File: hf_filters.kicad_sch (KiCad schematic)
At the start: 69 parts, among them J2 FILT_IN, J3 To CTRL:FILT_L, J4 UF1_OUT, J5 UF1_IN, J6 FILT_OUT, K10 EC2-5SNU, K11 EC2-5SNU, K4 EC2-5SNU, K5 EC2-5SNU, K6 EC2-5SNU, K7 EC2-5SNU, K8 EC2-5SNU, K9 EC2-5SNU, U4 ULN2803A, U5 74HC596

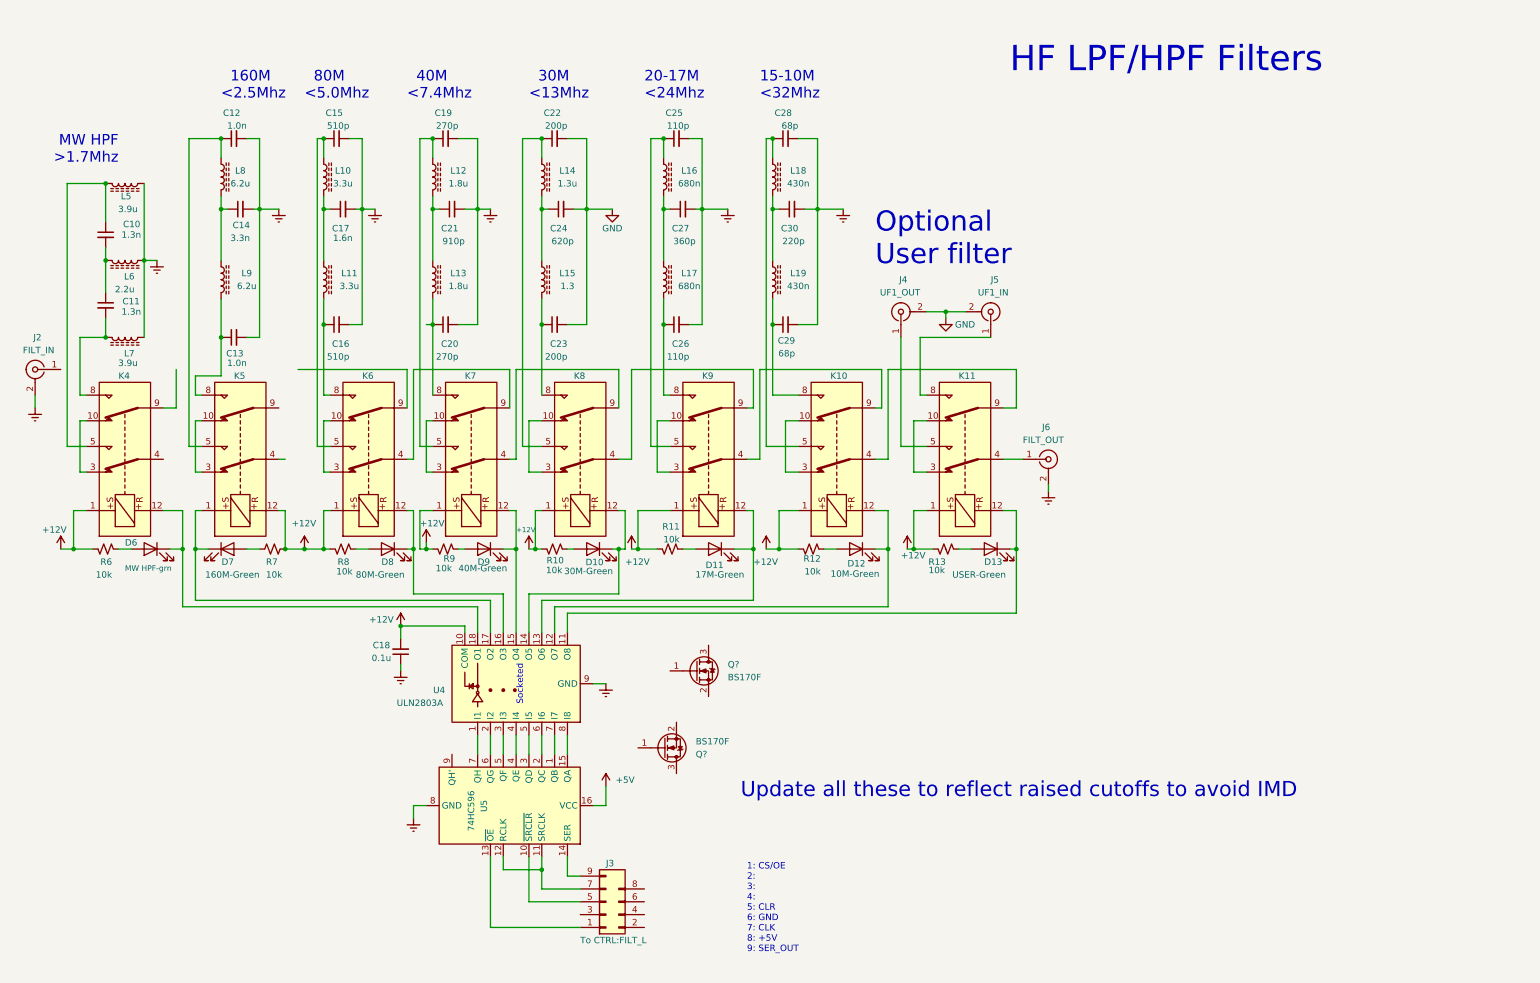
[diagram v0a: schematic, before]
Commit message: Replaced 74hc596 parts with mcp23017 and mcp23008 parts to simplify routing and reduce external parts count.
Added interface connectors for eventualy VHF (6m/2m/1.25m) RF path board.

Attempted to create some sort of documentations...
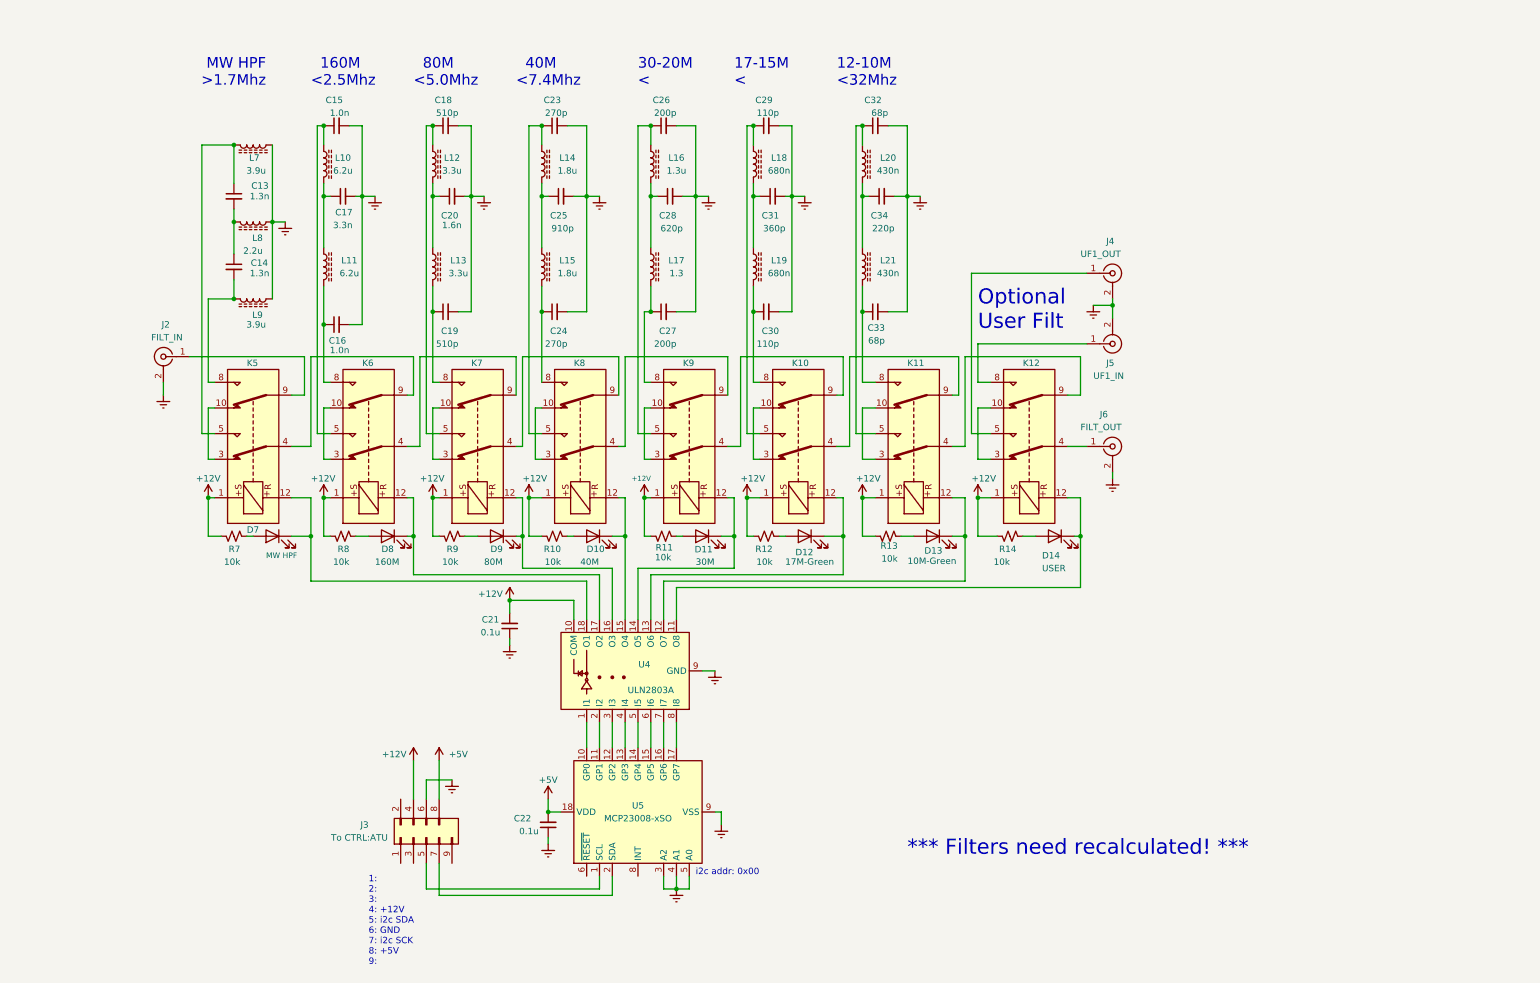
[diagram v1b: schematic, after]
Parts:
- removed Q? (x2): BS170F, Package_TO_SOT_SMD:SOT-23, symbol Transistor_FET:BS170F
- removed U5: 74HC596, Package_SO:TSSOP-16_4.4x5mm_P0.65mm, symbol 74xx:74HC596
- added C22: 0.1u, Capacitor_THT:C_Disc_D4.7mm_W2.5mm_P5.00mm, symbol Device:C_Small
- added U5: MCP23008-xSO, Package_SO:SOIC-18W_7.5x11.6mm_P1.27mm, symbol Interface_Expansion:MCP23008-xSO
- D10: renamed from D9; value 40M-Green -> 40M
- D11: renamed from D10; value 30M-Green -> 30M
- D14: renamed from D13; value USER-Green -> USER
- D7: renamed from D6; value MW HPF-grn -> MW HPF
- D8: renamed from D7; value 160M-Green -> 160M
- D9: renamed from D8; value 80M-Green -> 80M
- J3: value To CTRL:FILT_L -> To CTRL:ATU
- renumbered C10 to C13, C11 to C14, C12 to C15, C13 to C16, C14 to C17, C15 to C18, C16 to C19, C17 to C20, C18 to C21, C19 to C23, C20 to C24, C21 to C25, C22 to C26, C23 to C27, C24 to C28, C25 to C29, C26 to C30, C27 to C31, C28 to C32, C29 to C33, C30 to C34, D11 to D12, D12 to D13, K9 to K10, K10 to K11, K11 to K12, K4 to K5, K5 to K6, K6 to K7, K7 to K8, K8 to K9, L8 to L10, L9 to L11, L10 to L12, L11 to L13, L12 to L14, L13 to L15, L14 to L16, L15 to L17, L16 to L18, L17 to L19, L18 to L20, L19 to L21, L5 to L7, L6 to L8, L7 to L9, R9 to R10, R10 to R11, R11 to R12, R12 to R13, R13 to R14, R6 to R7, R7 to R8, R8 to R9
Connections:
- net GND is gone; now on net Earth: C26.2, C27.2, C28.2, J4.2 (Ext), J5.2 (Ext)
- net +12V: now also J3.4 (Pin_4), K6.1; no longer K6.12
- net +5V: now also J3.8 (Pin_8), C22.2, U5.18 (VDD)
- net Earth: now also J3.6 (Pin_6), C22.1, U5.3 (A2), U5.4 (A1), U5.5 (A0), U5.9 (VSS)
- net at D8.1 (K), U4.17 (O2): now also K6.12; no longer K6.1
- net at K6.4: now also K7.9
- net at K6.9: now also K5.4
- net at U4.7 (I7): now also U5.16 (GP6)
- net at J3.5 (Pin_5): now also U5.1 (SCL)
- net at J3.7 (Pin_7): now also U5.2 (SDA)
- net at U4.8 (I8): now also U5.17 (GP7)
- net at U4.6 (I6): now also U5.15 (GP5)
- net at U4.5 (I5): now also U5.14 (GP4)
- net at U4.4 (I4): now also U5.13 (GP3)
- net at U4.3 (I3): now also U5.12 (GP2)
- net at U4.2 (I2): now also U5.11 (GP1)
- net at U4.1 (I1): now also U5.10 (GP0)
- net at J2.1 (In): now also K5.9
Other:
- note added: "*** Filters need recalculated! ***"
- note added: "12-10M <32Mhz"
- note added: "17-15M <"
- note added: "1: 2: 3: 4: +12V 5: i2c SDA 6: GND 7: i2c SCK 8: +5V 9:"
- note added: "30-20M <"
- note added: "Optional User Filt"
- note added: "i2c addr: 0x00"
- note removed: "15-10M <32Mhz"
- note removed: "1: CS/OE 2: 3: 4: 5: CLR 6: GND 7: CLK 8: +5V 9: SER_OUT"
- note removed: "20-17M <24Mhz"
- note removed: "30M <13Mhz"
- note removed: "HF LPF/HPF Filters"
- note removed: "Optional User filter"
- note removed: "Socketed"
- note removed: "Update all these to reflect raised cutoffs to avoid IMD"
- moved on the sheet: C13, C14, C15, C16, C17, C18, C19, C20, C21, C23, C24, C25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

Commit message: cleanup of schematic and some initial firmware works...
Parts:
- removed C13: 1.3n, symbol Device:C_Small
- removed C22: 0.1u, Capacitor_THT:C_Disc_D4.7mm_W2.5mm_P5.00mm, symbol Device:C_Small
- removed D7: MW HPF, symbol Device:LED
- removed J2: FILT_IN, symbol Connector:Conn_Coaxial
- removed K5: EC2-5SNU, Relay_THT:Relay_DPDT_Kemet_EC2, symbol Relay:EC2-5SNU
- removed L7, L9: 3.9u, symbol Device:L_Ferrite
- removed R7: 10k, symbol Device:R_Small_US
- removed U5: MCP23008-xSO, Package_SO:SOIC-18W_7.5x11.6mm_P1.27mm, symbol Interface_Expansion:MCP23008-xSO
- added C23, C24, C25, C26, C27, C28, C29: 0.1u, Capacitor_THT:C_Disc_D4.7mm_W2.5mm_P5.00mm, symbol Device:C_Small
- added C30, C31, C32, C33, C34, C35, C36, C37, C38, C39, C7: 1.3n, symbol Device:C_Small
- added D1, D62: USER2, symbol Device:LED
- added D10, D11, D12, D13, D9: MW HPF, symbol Device:LED
- added J3: TX_FILT_IN, symbol Connector:Conn_Coaxial
- added J37: UTF2_OUT, symbol Connector:Conn_Coaxial
- added J38: TX_FILT_OUT, symbol Connector:Conn_Coaxial
- added J4: UTF2_IN, symbol Connector:Conn_Coaxial
- added J7: RX_FILT_IN, symbol Connector:Conn_Coaxial
- added K1, K10, K11, K12, K13, K45, K9: EC2-5SNU, Relay_THT:Relay_DPDT_Kemet_EC2, symbol Relay:EC2-5SNU
- added L1, L15, L16, L17, L18, L19, L20, L26, L27, L28, L29, L30: 3.9u, symbol Device:L_Ferrite
- added L21, L22, L23, L24, L25: 2.2u, symbol Device:L_Ferrite
- added R1, R10, R11, R12, R13, R87, R9: 10k, symbol Device:R_Small_US
- added U2: MCP23017_SO, Package_SO:SOIC-28W_7.5x17.9mm_P1.27mm, symbol Interface_Expansion:MCP23017_SO
- added U3: ULN2803A, symbol Transistor_Array:ULN2803A
- D2: renamed from D14; value USER -> USER1
- D3: renamed from D13; value 10M-Green -> 12-10M
- D4: renamed from D12; value 17M-Green -> 17-15M
- D5: renamed from D11; value 30M -> 30-20M
- J1: renamed from J5; value UF1_IN -> UTF1_IN
- J2: renamed from J4; value UF1_OUT -> UTF1_OUT
- J5: renamed from J3; value To CTRL:ATU -> To CTRL_FILT
- J6: value FILT_OUT -> RX_FILT_OUT
- renumbered C32 to C1, C28 to C10, C25 to C11, C20 to C12, C17 to C13, C33 to C15, C30 to C16, C27 to C17, C24 to C18, C29 to C2, C16 to C20, C26 to C3, C23 to C4, C18 to C5, C15 to C6, C34 to C8, C31 to C9, D10 to D6, D9 to D7, K12 to K2, K11 to K3, K10 to K4, K9 to K5, K8 to K6, K6 to K8, L19 to L10, L17 to L11, L15 to L12, L11 to L14, L20 to L2, L18 to L3, L16 to L4, L14 to L5, L12 to L6, L10 to L7, L21 to L9, R14 to R2, R13 to R3, R12 to R4, R11 to R5, R10 to R6, R9 to R7, U4 to U1
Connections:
- net +12V: now also K1.1, K10.1, K11.1, K12.1, K13.1, K45.1, K9.1, R1.1, R10.1, R11.1, R12.1, R13.1, R87.1, R9.1; no longer J5.4 (Pin_4)
- net +5V: now also C23.2, C24.2, U2.9 (VDD), U3.10 (COM); no longer J5.8 (Pin_8)
- net Earth: now also C23.1, C24.1, C25.2, C26.2, C27.2, C28.2, C29.2, J3.2 (Ext), J37.2 (Ext), J38.2 (Ext), J4.2 (Ext), J7.1 (In), L1.2, L15.2, L16.2, L17.2, L18.2, L19.2, L20.2, L21.2, L22.2, L23.2, L24.2, L25.2, L26.2, L27.2, L28.2, L29.2, L30.2, U2.10 (VSS), U2.15 (A0), U2.16 (A1), U2.17 (A2), U3.9 (GND)
- net at C14.2: now also K1.8, L15.1
- net at D2.1 (K), K2.12: now also U1.12 (O7); no longer U1.11 (O8)
- net at K2.4: now also K45.9; no longer J6.1 (In)
- net at J5.5 (Pin_5): now also U2.13 (SDA)
- net at J5.7 (Pin_7): now also U2.12 (SCK)
- net at U1.18 (O1): now also D8.1 (K), K8.12
- net at D5.1 (K), K5.12: now also U1.15 (O4); no longer U1.14 (O5)
- net at K8.9: now also J3.1 (In)
- net at C14.1, L8.1: now also C7.2
- net at U1.1 (I1): now also U2.21 (GPA0)
- net at U1.2 (I2): now also U2.22 (GPA1)
- net at U1.3 (I3): now also U2.23 (GPA2)
- net at U1.4 (I4): now also U2.24 (GPA3)
- net at U1.5 (I5): now also U2.25 (GPA4)
- net at U1.6 (I6): now also U2.26 (GPA5)
- net at U1.7 (I7): now also U2.27 (GPA6)
- net at U1.8 (I8): now also U2.28 (GPA7)
- net at D3.1 (K), K3.12: now also U1.13 (O6); no longer U1.12 (O7)
- net at D4.1 (K), K4.12: now also U1.14 (O5); no longer U1.13 (O6)
- net at D6.1 (K), K6.12: now also U1.16 (O3); no longer U1.15 (O4)
- net at D7.1 (K), K7.12: now also U1.17 (O2); no longer U1.16 (O3)
- new net: C29.1, D13.1 (K), K13.12, U3.14 (O5)
- new net: D13.2 (A), R13.2
- new net: C25.1, D9.1 (K), K9.12, U3.18 (O1)
- new net: D1.1 (K), K1.12, U3.13 (O6)
- new net: D1.2 (A), R1.2
- new net: C33.1, C38.2, L24.1
- new net: C33.2, K12.8, L19.1
- new net: C34.2, K13.8, L20.1
- new net: K13.10, K13.3
- new net: K1.4, K13.4
- new net: C39.1, K13.5, L30.1
- new net: K12.4, K13.9
- new net: C38.1, K12.5, L29.1
- new net: D9.2 (A), R9.2
- new net: C36.1, K10.5, L27.1
- new net: C26.1, D10.1 (K), K10.12, U3.17 (O2)
- new net: C28.1, D12.1 (K), K12.12, U3.15 (O4)
- new net: D12.2 (A), R12.2
- new net: C34.1, C39.2, L25.1
- new net: C30.1, C35.2, L21.1
- new net: C30.2, K9.8, L16.1
- new net: C32.1, C37.2, L23.1
- new net: C32.2, K11.8, L18.1
- new net: C31.2, K10.8, L17.1
- new net: K9.10, K9.3
- new net: K10.9, K9.4
- new net: C35.1, K9.5, L26.1
- new net: J6.1 (In), K9.9
- new net: C31.1, C36.2, L22.1
- new net: D62.1 (K), K45.12, U1.11 (O8)
- new net: D62.2 (A), R87.2
- new net: K10.10, K10.3
- new net: K10.4, K11.9
- new net: U2.1 (GPB0), U3.1 (I1)
- new net: C27.1, D11.1 (K), K11.12, U3.16 (O3)
- new net: U2.2 (GPB1), U3.2 (I2)
- new net: U2.3 (GPB2), U3.3 (I3)
- new net: U2.4 (GPB3), U3.4 (I4)
- new net: U2.5 (GPB4), U3.5 (I5)
- new net: U2.6 (GPB5), U3.6 (I6)
- new net: U2.7 (GPB6), U3.7 (I7)
- new net: U2.8 (GPB7), U3.8 (I8)
- new net: K11.10, K11.3
- new net: K11.4, K12.9
- new net: C37.1, K11.5, L28.1
- new net: C7.1, K1.5, L1.1
- new net: K12.10, K12.3
- new net: J4.1 (In), K45.8
- new net: D11.2 (A), R11.2
- new net: J7.2 (Ext), K1.9
- new net: K45.10, K45.3
- new net: J38.1 (In), K45.4
- new net: J37.1 (In), K45.5
- new net: K1.10, K1.3
- new net: D10.2 (A), R10.2
- no-connect marks 0 -> 13
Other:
- note added: "12-10M BPF"
- note added: "160-80M BPF"
- note added: "17-15M BPF"
- note added: "30-20M BPF"
- note added: "4: +12V 5: i2c SDA 6: GND 7: i2c SCK 8: +5V"
- note added: "60-40M BPF"
- note added: "Opt. User HF TX Filt 1"
- note added: "Opt. User HF TX Filt 2"
- note removed: "1: 2: 3: 4: +12V 5: i2c SDA 6: GND 7: i2c SCK 8: +5V 9:"
- note removed: "Optional User Filt"
- title: HF Filters -> HF TX/RX Filters
- moved on the sheet: C1, C10, C11, C12, C13, C15, C16, C17, C18, C19, C2, C20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

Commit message: cleanup
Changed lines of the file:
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@@
     (effects (font (size 2.1 2.1)) (justify left bottom))
   )
-  (text "*** Filters need recalculated! ***" (at 198.12 176.53 0)
+  (text "*** Filters need recalculated! ***" (at 195.58 175.26 0)
     (effects (font (size 3 3)) (justify left bottom))
   )

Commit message: cleanup and trying to implement stubs for future features
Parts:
- D1: value USER2 -> MW HPF
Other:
- moved on the sheet: C24, J5
